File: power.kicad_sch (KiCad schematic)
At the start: 95 parts, among them J1 Molex_Nano-Fit_1x2_SMD_105430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, J2 USB-C_GCT_USB4105-GF-A, Q1 2N7002_SOT-23-3, U1 TPS566231P, U2 TPS566231P, U3 TPS566231P, U4 TPS566231P, U5 TPS566231P

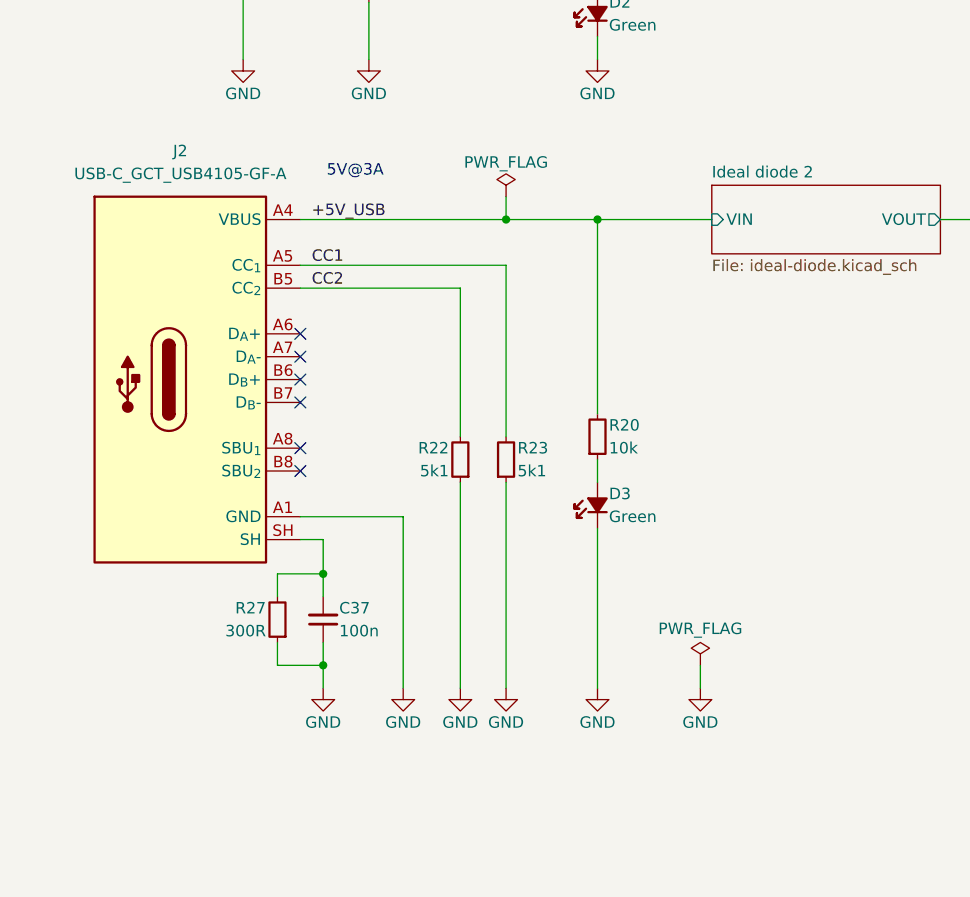
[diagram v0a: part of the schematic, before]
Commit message: [#86617] Unify captions, add TVS to USB VBUS
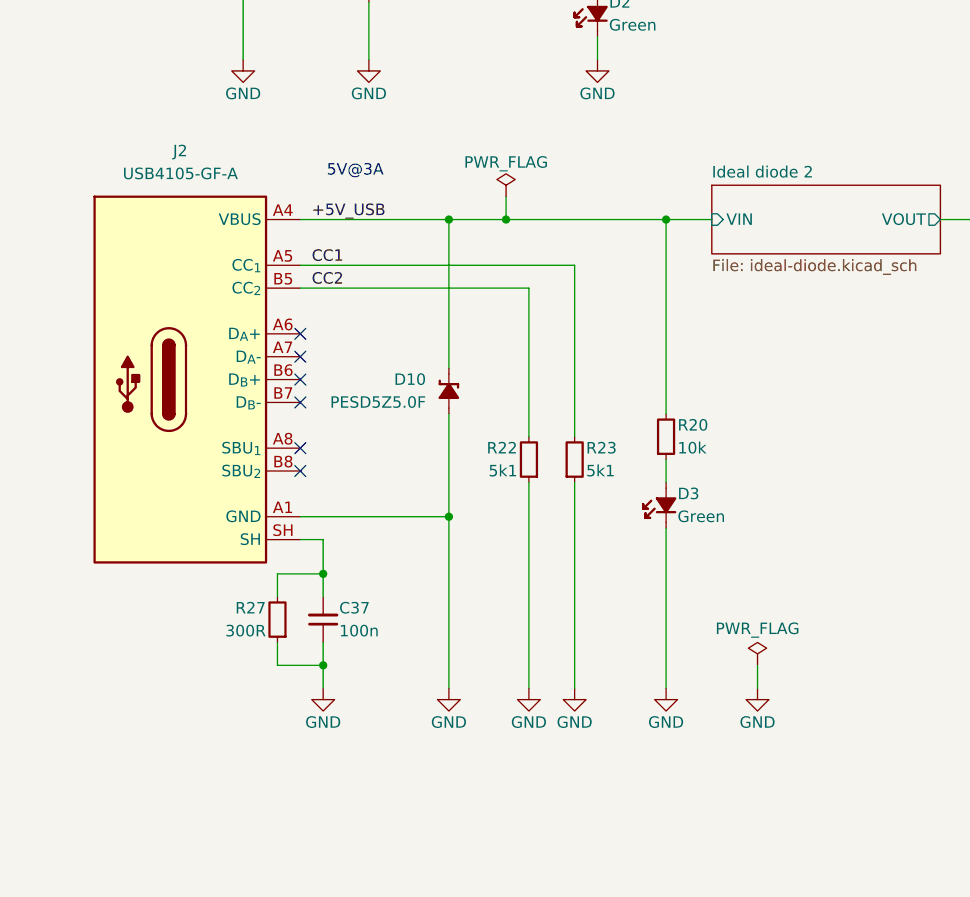
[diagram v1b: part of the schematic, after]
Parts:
- added D10: PESD5Z5_0F, antmicro-footprints:SOD-523, symbol antmicroTVSDiodes:PESD5Z5_0F
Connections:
- net +5V_USB: now also D10.1 (C)
- net GND: now also D10.2 (A)
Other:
- moved on the sheet: D3, R20, R22, R23

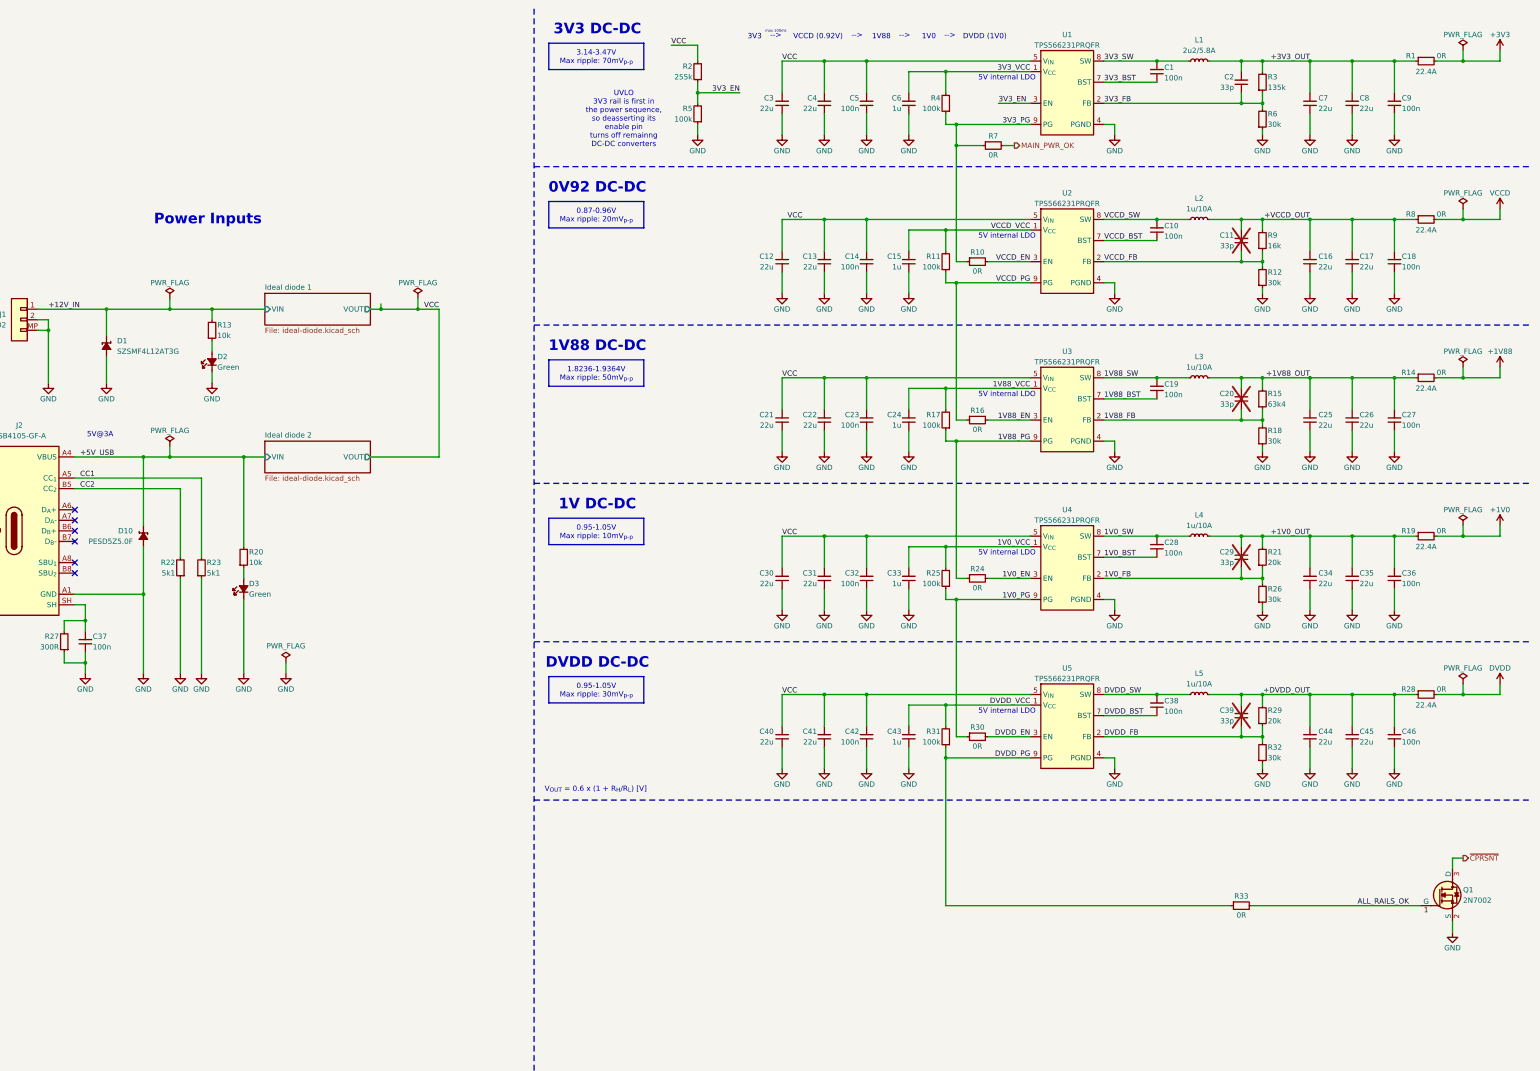
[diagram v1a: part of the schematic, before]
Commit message: [#86617] Add PWR test-points and PGOOD LED, fix MAIN_PWR_OK voltage level
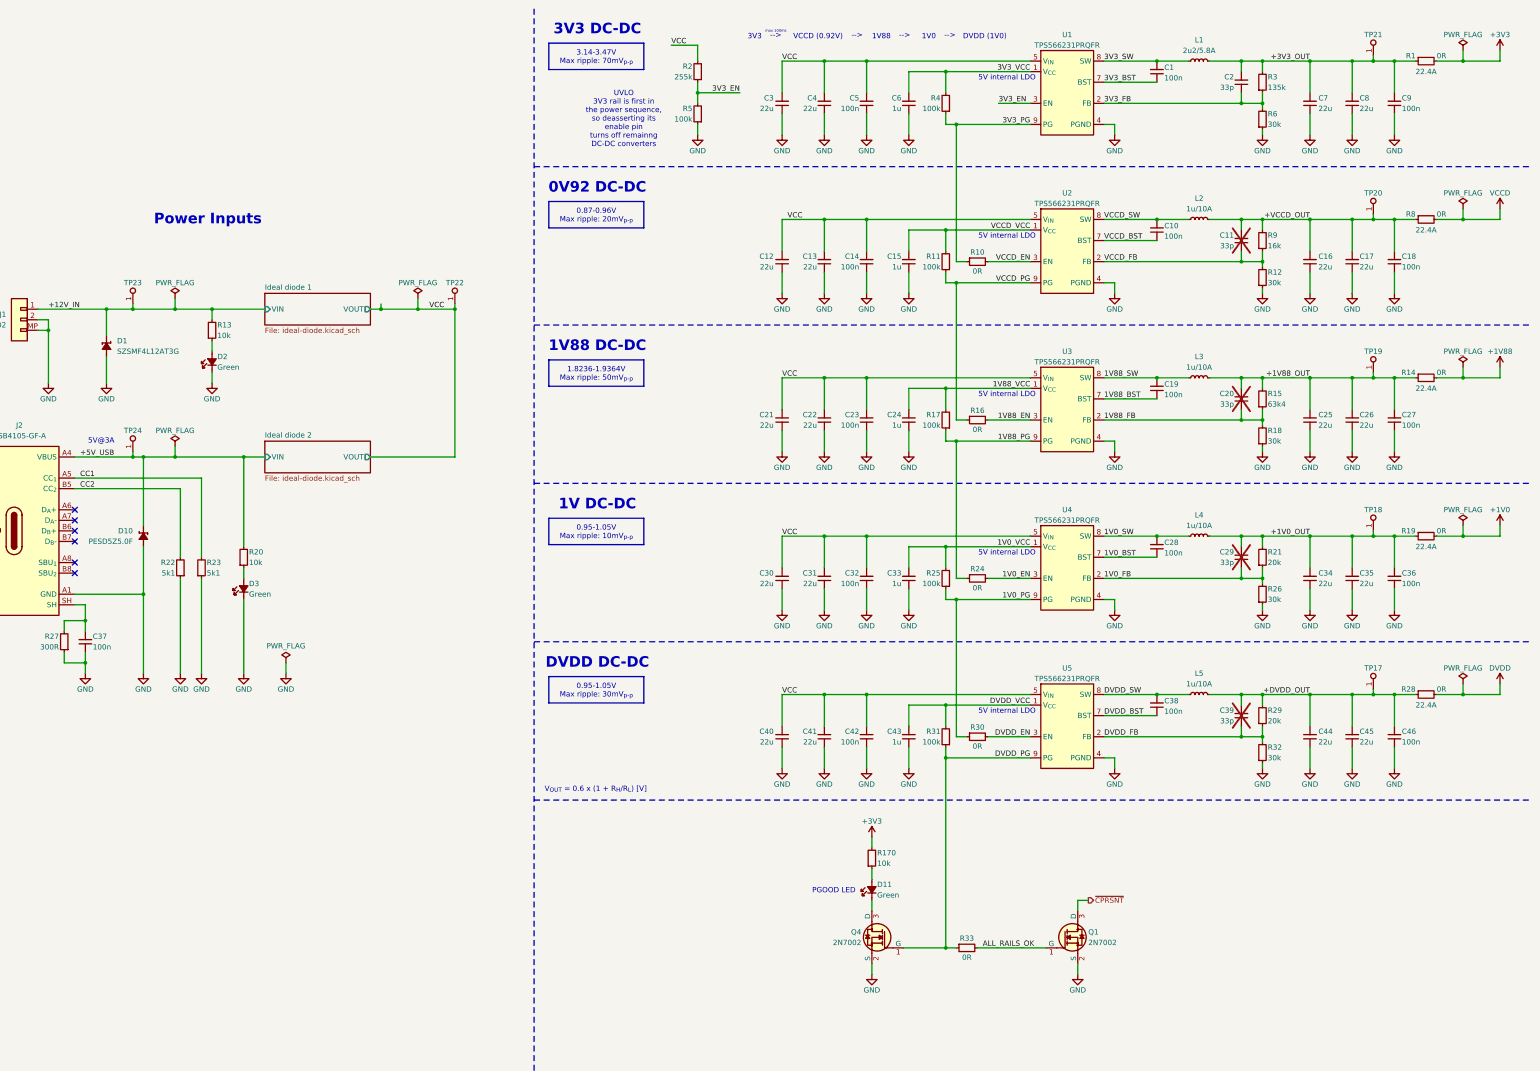
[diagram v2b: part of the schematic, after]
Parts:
- removed R7: R_0R_0402, antmicro-footprints:R_0402_1005Metric, symbol antmicroResistors0402:R_0R_0402
- added D11: LED_G_0603_LG_L29K-G2J1-24-Z, antmicro-footprints:LED_0603_1608Metric_G, symbol antmicroLEDIndicationDiscrete:LED_G_0603_LG_L29K-G2J1-24-Z
- added Q4: 2N7002_SOT-23-3, antmicro-footprints:SOT-23-3, symbol antmicroTransistorsFETsMOSFETsSingle:2N7002_SOT-23-3
- added R170: R_10k_0402, antmicro-footprints:R_0402_1005Metric, symbol antmicroResistors0402:R_10k_0402
- added TP17, TP18, TP19, TP20, TP21, TP22, TP23, TP24: TP_0.75mm_SMD, antmicro-footprints:TP_SMD_0.75mm, symbol antmicroTestPoints:TP_0.75mm_SMD
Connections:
- net +12V_IN: now also TP23.1
- net +1V0_OUT: now also TP18.1
- net +1V88_OUT: now also TP19.1
- net +3V3: now also R170.2
- net +3V3_OUT: now also TP21.1
- net +5V_USB: now also TP24.1
- net +DVDD_OUT: now also TP17.1
- net +VCCD_OUT: now also TP20.1
- net DVDD_PG: now also Q4.1 (G)
- net GND: now also Q4.2 (S)
- net VCC: now also TP22.1
- new net: D11.1 (C), Q4.3 (D)
- new net: D11.2 (A), R170.1
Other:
- note added: "PGOOD LED"
- moved on the sheet: Q1, R33

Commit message: [#86617] Add more capacitance to DC-DC converters outputs
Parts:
- added C204, C205, C206, C207, C208: C_22u_16V_0603, antmicro-footprints:C_0603_1608Metric_EIA, symbol antmicroCapacitors0603:C_22u_16V_0603
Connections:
- net +1V0_OUT: now also C207.2
- net +1V88_OUT: now also C206.2
- net +3V3_OUT: now also C205.2
- net +DVDD_OUT: now also C208.2
- net +VCCD_OUT: now also C204.2
- net GND: now also C204.1, C205.1, C206.1, C207.1, C208.1
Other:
- moved on the sheet: C1, C10, C11, C12, C13, C14, C15, C16, C17, C19, C2, C20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

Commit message: [#86351] Rename project
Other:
- title: 10GbE Expansion -> OCuLink to 10GbE adapter

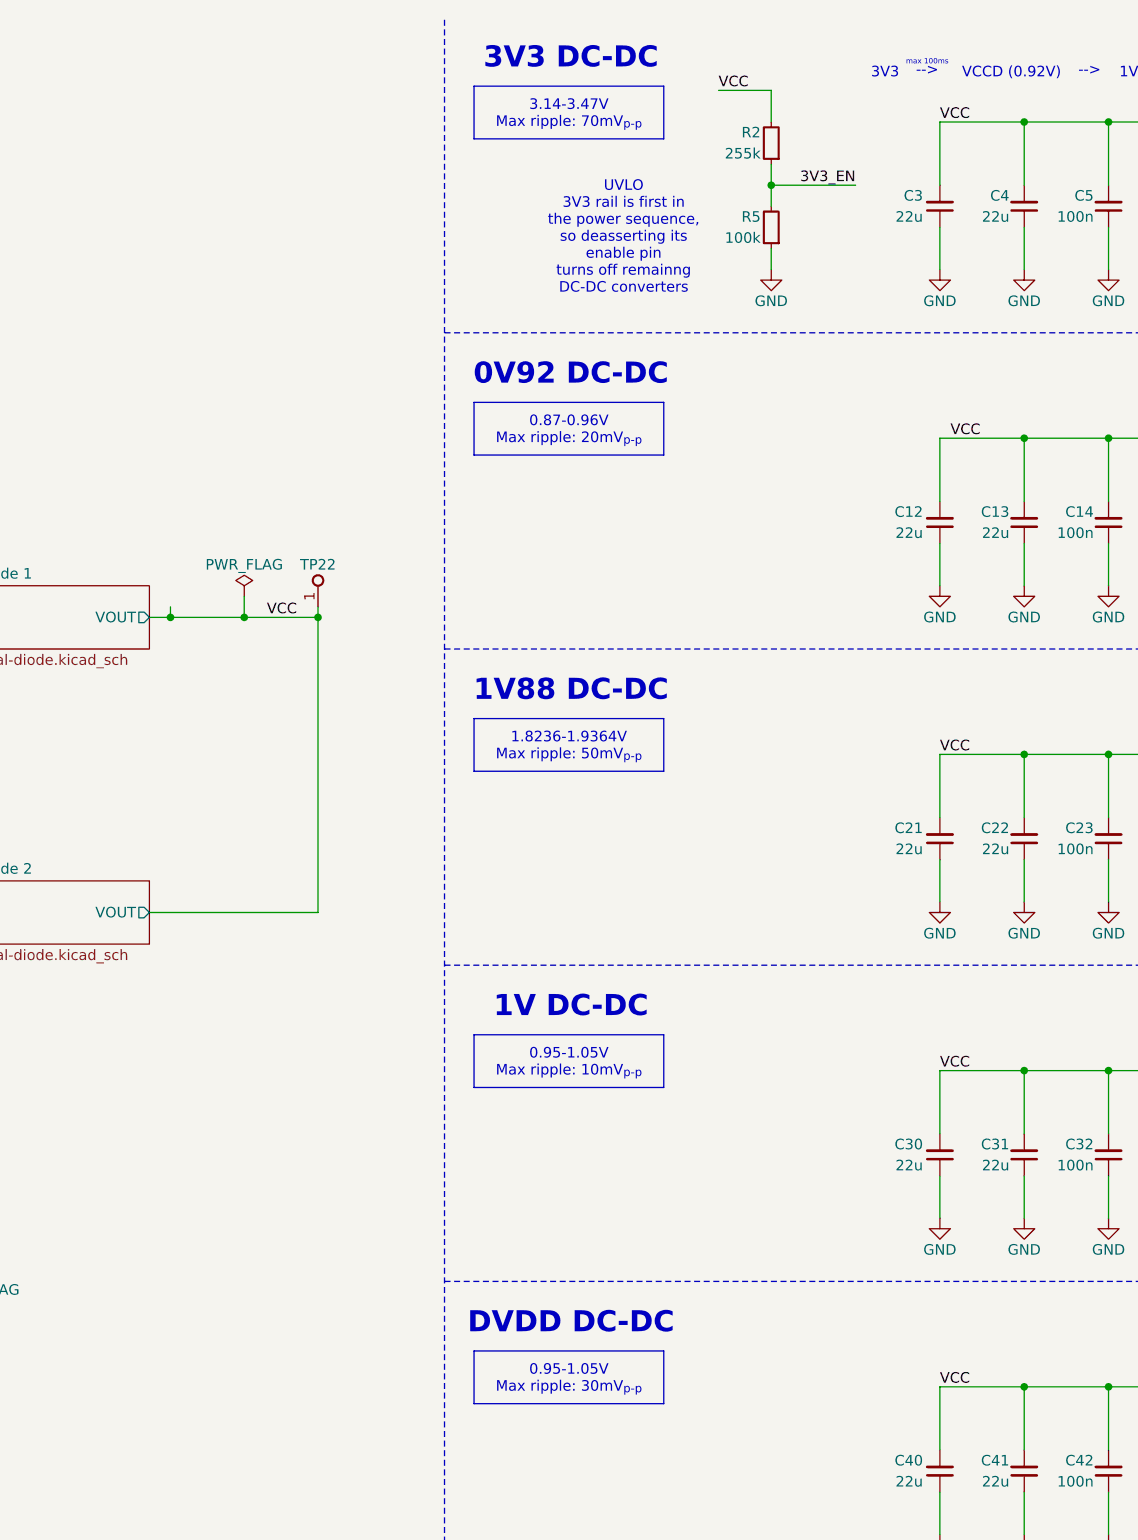
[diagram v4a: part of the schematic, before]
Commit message: [#86851] Add fan controller
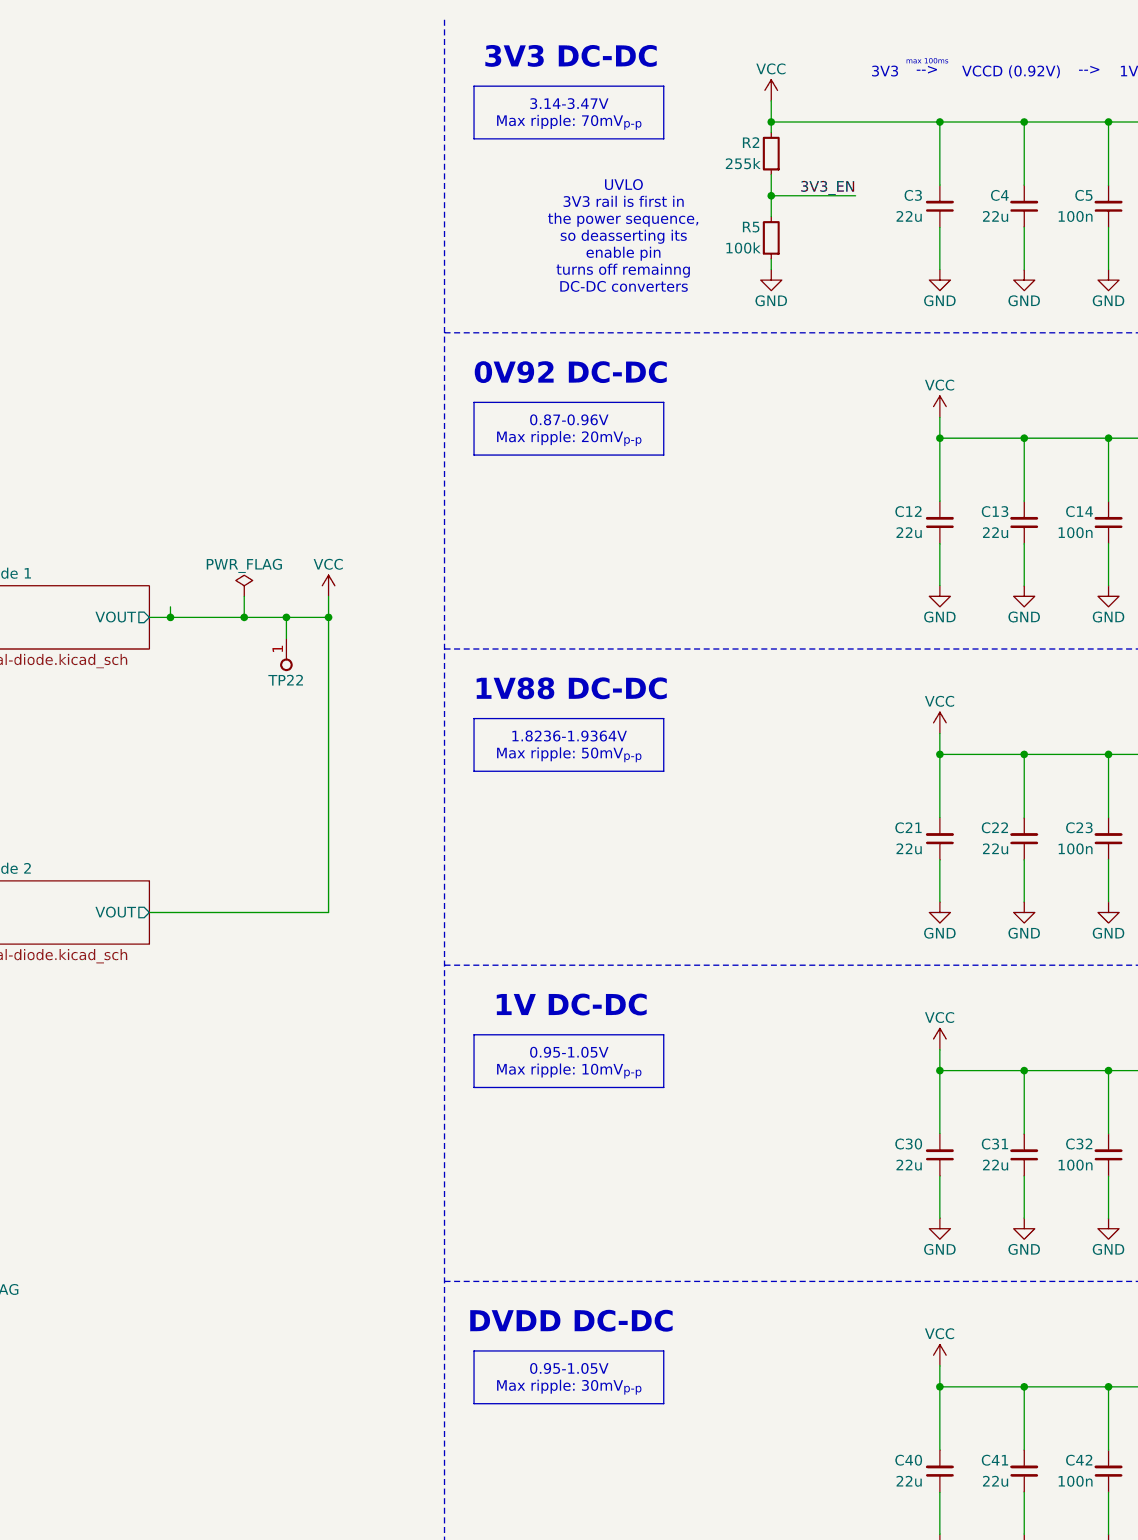
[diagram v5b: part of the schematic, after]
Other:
- moved on the sheet: R2, R5, TP22

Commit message: [#86351] Minor BOM consolidation
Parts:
- C37: value C_100n_16V_X7R_0402 -> C_100n_0402; symbol antmicroCapacitors0402:C_100n_16V_X7R_0402 -> antmicroCapacitors0402:C_100n_0402; Dielectric X7R -> X5R; MPN C0402C104J4RAC7411 -> GRM155R61H104KE14D; Manufacturer KEMET -> Murata; Voltage 16V -> 50V
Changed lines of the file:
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@@
 	)
 	(symbol
-		(lib_id "antmicroCapacitors0402:C_100n_16V_X7R_0402")
+		(lib_id "antmicroCapacitors0402:C_100n_0402")
 		(at 53.34 167.64 90)
 		(unit 1)
@@
 			)
 		)
-		(property "Value" "C_100n_16V_X7R_0402"
+		(property "Value" "C_100n_0402"
 			(at 76.2 152.4 0)
 			(effects
@@
 			)
 		)
-		(property "Datasheet" "https://www.kemet.com/en/us/capacitors/product/C0402C104J4RAC7411.html"
+		(property "Datasheet" "https://www.murata.com/products/productdetail?partno=GRM155R61H104KE14%23"
 			(at 81.28 152.4 0)
 			(effects
@@
 			)
 		)
-		(property "Description" "SMD Multilayer Ceramic Capacitor, 100nF, 50V, 0402, ±5%, X7R"
+		(property "Description" "SMD Multilayer Ceramic Capacitor, 0.1 µF, 50 V, 0402 [1005 Metric], ± 10%, X5R, GRM Series"
 			(at 53.34 167.64 0)
 			(effects
@@
 			)
 		)
-		(property "MPN" "C0402C104J4RAC7411"
+		(property "MPN" "GRM155R61H104KE14D"
 			(at 83.82 152.4 0)
 			(effects
@@
 			)
 		)
-		(property "Voltage" "16V"
+		(property "Voltage" "50V"
 			(at 63.5 152.4 0)
 			(effects
@@
 			)
 		)
-		(property "Dielectric" "X7R"
+		(property "Dielectric" "X5R"
 			(at 66.04 152.4 0)
 			(effects
@@
 			)
 		)
-		(property "Manufacturer" "KEMET"
+		(property "Manufacturer" "Murata"
 			(at 68.58 152.4 0)
 			(effects
